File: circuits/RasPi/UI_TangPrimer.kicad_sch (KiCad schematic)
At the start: 10 parts, among them SW6 SW_SPDT

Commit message: PDFプロット
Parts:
- D12, D13, D14, D15: value Red -> Blue
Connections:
- net LED0 renamed LED_B0
- net LED1 renamed LED_B1
- net LED2 renamed LED_B2
- net LED3 renamed LED_B3
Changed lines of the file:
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@@
     (stroke (width 0) (type default))
   )
-  (polyline (pts (xy 106.68 66.04) (xy 170.18 66.04))
+  (polyline (pts (xy 106.68 63.5) (xy 170.18 63.5))
     (stroke (width 0.5) (type solid))
   )
@@
     (stroke (width 0.5) (type solid))
   )
-  (polyline (pts (xy 106.68 147.32) (xy 106.68 66.04))
+  (polyline (pts (xy 106.68 147.32) (xy 106.68 63.5))
     (stroke (width 0.5) (type solid))
   )
-  (polyline (pts (xy 170.18 147.32) (xy 170.18 66.04))
+  (polyline (pts (xy 170.18 147.32) (xy 170.18 63.5))
     (stroke (width 0.5) (type solid))
   )
@@
     (effects (font (size 1.27 1.27)) (justify left bottom))
   )
-  (text "LED" (at 109.22 71.12 0)
+  (text "LED" (at 109.22 68.58 0)
     (effects (font (size 1.27 1.27)) (justify left bottom))
   )
-  (text "I/O" (at 109.22 63.5 0)
+  (text "I/O" (at 109.22 60.96 0)
     (effects (font (size 2.54 2.54)) (justify left bottom))
   )
-  (hierarchical_label "LED2" (shape input) (at 127 93.98 180) (fields_autoplaced)
+  (hierarchical_label "LED_B2" (shape input) (at 127 93.98 180) (fields_autoplaced)
     (effects (font (size 1.27 1.27)) (justify right))
   )
@@
     (effects (font (size 1.27 1.27)) (justify left))
   )
-  (hierarchical_label "LED0" (shape input) (at 127 73.66 180) (fields_autoplaced)
+  (hierarchical_label "LED_B0" (shape input) (at 127 73.66 180) (fields_autoplaced)
     (effects (font (size 1.27 1.27)) (justify right))
   )
-  (hierarchical_label "LED3" (shape input) (at 127 104.14 180) (fields_autoplaced)
+  (hierarchical_label "LED_B3" (shape input) (at 127 104.14 180) (fields_autoplaced)
     (effects (font (size 1.27 1.27)) (justify right))
   )
-  (hierarchical_label "LED1" (shape input) (at 127 83.82 180) (fields_autoplaced)
+  (hierarchical_label "LED_B1" (shape input) (at 127 83.82 180) (fields_autoplaced)
     (effects (font (size 1.27 1.27)) (justify right))
   )
@@
       (effects (font (size 1.27 1.27)))
     )
-    (property "Value" "Red" (at 144.78 96.52 0)
+    (property "Value" "Blue" (at 144.78 96.52 0)
       (effects (font (size 1.27 1.27)))
     )
@@
       (effects (font (size 1.27 1.27)))
     )
-    (property "Value" "Red" (at 144.78 86.36 0)
+    (property "Value" "Blue" (at 144.78 86.36 0)
       (effects (font (size 1.27 1.27)))
     )
@@
       (effects (font (size 1.27 1.27)))
     )
-    (property "Value" "Red" (at 144.78 76.2 0)
+    (property "Value" "Blue" (at 144.78 76.2 0)
       (effects (font (size 1.27 1.27)))
     )
@@
       (effects (font (size 1.27 1.27)))
     )
-    (property "Value" "Red" (at 144.78 106.68 0)
-      (effects (font (size 1.27 1.27)))
-    )
+    (property "Value" "Blue" (at 144.78 106.68 0)
+      (effects (font (size 1.27 1.27)))
+    )

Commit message: シンボル・フットプリントMyLib->TomoshibiLib置き換え
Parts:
- SW6: footprint MyLibrary:SW_Slide_3P_SPDT -> TomoshibiLibrary:SW_Slide_3P_SPDT
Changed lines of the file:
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@@
       (effects (font (size 1.27 1.27)) (justify left))
     )
-    (property "Footprint" "MyLibrary:SW_Slide_3P_SPDT" (at 132.08 129.54 0)
+    (property "Footprint" "TomoshibiLibrary:SW_Slide_3P_SPDT" (at 132.08 129.54 0)
       (effects (font (size 1.27 1.27)) hide)
     )

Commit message: 更新
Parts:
- SW6: footprint TomoshibiLibrary:SW_Slide_3P_SPDT -> TomoshibiLibrary:SW_Slide_SPDT_SSSS213202
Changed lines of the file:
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@@
+    )
+  )
+  (symbol (lib_id "Switch:SW_SPDT") (at 132.08 129.54 0) (mirror x) (unit 1)
+    (in_bom yes) (on_board yes) (dnp no)
+    (property "Reference" "SW6" (at 124.46 136.9314 0)
+      (effects (font (size 1.27 1.27)) (justify left))
+    )
+    (property "Value" "SW_SPDT" (at 124.46 134.62 0)
+      (effects (font (size 1.27 1.27)) (justify left))
+    )
+    (property "Footprint" "TomoshibiLibrary:SW_Slide_SPDT_SSSS213202" (at 132.08 129.54 0)
+      (effects (font (size 1.27 1.27)) hide)
+    )
+    (property "Datasheet" "~" (at 132.08 129.54 0)
+      (effects (font (size 1.27 1.27)) hide)
+    )
+    (pin "1")
+    (pin "2")
+    (pin "3")
+    (instances
+      (project "RasPi"
+        (path "/689a9e74-f202-4ea4-bfbb-4341f2549250/a0e6e20f-c732-4650-b515-927ea2aa6bd5/e4ed8e7b-a26f-475c-8428-58a8505b00cf"
+          (reference "SW6") (unit 1)
+        )
+      )
     )
   )
@@
         )
       )
-    )
-  )
-  (symbol (lib_id "Switch:SW_SPDT") (at 132.08 129.54 0) (mirror x) (unit 1)
-    (in_bom yes) (on_board yes) (dnp no)
-    (property "Reference" "SW6" (at 124.46 136.9314 0)
-      (effects (font (size 1.27 1.27)) (justify left))
-    )
-    (property "Value" "SW_SPDT" (at 124.46 134.62 0)
-      (effects (font (size 1.27 1.27)) (justify left))
-    )
-    (property "Footprint" "TomoshibiLibrary:SW_Slide_3P_SPDT" (at 132.08 129.54 0)
-      (effects (font (size 1.27 1.27)) hide)
-    )
-    (property "Datasheet" "~" (at 132.08 129.54 0)
-      (effects (font (size 1.27 1.27)) hide)
-    )
-    (pin "1")
-    (pin "2")
-    (pin "3")
-    (instances
-      (project "RasPi"
-        (path "/689a9e74-f202-4ea4-bfbb-4341f2549250/a0e6e20f-c732-4650-b515-927ea2aa6bd5/e4ed8e7b-a26f-475c-8428-58a8505b00cf"
-          (reference "SW6") (unit 1)
-        )
-      )

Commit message: raspi基板回路図
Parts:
- added H1, H2, H3, H4: MountingHole_Pad, TestPoint:TestPoint_Pad_1.0x1.0mm, symbol Mechanical:MountingHole_Pad
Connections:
- net LED_B0: now also H1.1
- net LED_B1: now also H2.1
- net LED_B2: now also H3.1
- net LED_B3: now also H4.1
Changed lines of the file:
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@@
 (kicad_sch (version 20230121) (generator eeschema)
   (paper "A4")
+  (junction (at 129.54 93.98) (diameter 0) (color 0 0 0 0)
+  )
   (junction (at 139.7 132.08) (diameter 0) (color 0 0 0 0)
   )
+  (junction (at 129.54 83.82) (diameter 0) (color 0 0 0 0)
+  )
+  (junction (at 129.54 104.14) (diameter 0) (color 0 0 0 0)
+  )
+  (junction (at 129.54 73.66) (diameter 0) (color 0 0 0 0)
+  )
   (no_connect (at 137.16 127))
+  (wire (pts (xy 129.54 83.82) (xy 130.81 83.82))
+    (stroke (width 0) (type default))
+  )
   (wire (pts (xy 124.46 129.54) (xy 127 129.54))
     (stroke (width 0) (type default))
@@
     (stroke (width 0) (type default))
   )
-  (wire (pts (xy 127 93.98) (xy 130.81 93.98))
-    (stroke (width 0) (type default))
-  )
-  (wire (pts (xy 127 83.82) (xy 130.81 83.82))
-    (stroke (width 0) (type default))
-  )
-  (wire (pts (xy 127 104.14) (xy 130.81 104.14))
+  (wire (pts (xy 127 93.98) (xy 129.54 93.98))
+    (stroke (width 0) (type default))
+  )
+  (wire (pts (xy 127 83.82) (xy 129.54 83.82))
+    (stroke (width 0) (type default))
+  )
+  (wire (pts (xy 127 104.14) (xy 129.54 104.14))
     (stroke (width 0) (type default))
   )
@@
     (stroke (width 0.5) (type solid))
   )
+  (wire (pts (xy 129.54 73.66) (xy 130.81 73.66))
+    (stroke (width 0) (type default))
+  )
   (polyline (pts (xy 170.18 147.32) (xy 170.18 63.5))
     (stroke (width 0.5) (type solid))
@@
     (stroke (width 0) (type default))
   )
-  (wire (pts (xy 127 73.66) (xy 130.81 73.66))
+  (wire (pts (xy 129.54 104.14) (xy 130.81 104.14))
+    (stroke (width 0) (type default))
+  )
+  (wire (pts (xy 127 73.66) (xy 129.54 73.66))
+    (stroke (width 0) (type default))
+  )
+  (wire (pts (xy 129.54 93.98) (xy 130.81 93.98))
     (stroke (width 0) (type default))
   )
@@
     )
   )
+  (symbol (lib_id "Mechanical:MountingHole_Pad") (at 129.54 91.44 0) (mirror y) (unit 1)
+    (in_bom yes) (on_board yes) (dnp no)
+    (property "Reference" "H3" (at 114.3 88.9 0)
+      (effects (font (size 1.27 1.27)) (justify right))
+    )
+    (property "Value" "MountingHole_Pad" (at 114.3 86.36 0)
+      (effects (font (size 1.27 1.27)) (justify right))
+    )
+    (property "Footprint" "TestPoint:TestPoint_Pad_1.0x1.0mm" (at 129.54 91.44 0)
+      (effects (font (size 1.27 1.27)) hide)
+    )
+    (property "Datasheet" "~" (at 129.54 91.44 0)
+      (effects (font (size 1.27 1.27)) hide)
+    )
+    (pin "1")
+    (instances
+      (project "RasPi"
+        (path "/689a9e74-f202-4ea4-bfbb-4341f2549250/a0e6e20f-c732-4650-b515-927ea2aa6bd5/e4ed8e7b-a26f-475c-8428-58a8505b00cf"
+          (reference "H3") (unit 1)
+        )
+      )
+    )
+  )
   (symbol (lib_id "power:GNDD") (at 152.4 73.66 0) (unit 1)
     (in_bom yes) (on_board yes) (dnp no) (fields_autoplaced)
@@
     )
   )
+  (symbol (lib_id "Mechanical:MountingHole_Pad") (at 129.54 81.28 0) (mirror y) (unit 1)
+    (in_bom yes) (on_board yes) (dnp no)
+    (property "Reference" "H2" (at 114.3 78.74 0)
+      (effects (font (size 1.27 1.27)) (justify right))
+    )
+    (property "Value" "MountingHole_Pad" (at 114.3 76.2 0)
+      (effects (font (size 1.27 1.27)) (justify right))
+    )
+    (property "Footprint" "TestPoint:TestPoint_Pad_1.0x1.0mm" (at 129.54 81.28 0)
+      (effects (font (size 1.27 1.27)) hide)
+    )
+    (property "Datasheet" "~" (at 129.54 81.28 0)
+      (effects (font (size 1.27 1.27)) hide)
+    )
+    (pin "1")
+    (instances
+      (project "RasPi"
+        (path "/689a9e74-f202-4ea4-bfbb-4341f2549250/a0e6e20f-c732-4650-b515-927ea2aa6bd5/e4ed8e7b-a26f-475c-8428-58a8505b00cf"
+          (reference "H2") (unit 1)
+        )
+      )
+    )
+  )
   (symbol (lib_id "power:GNDD") (at 152.4 83.82 0) (unit 1)
     (in_bom yes) (on_board yes) (dnp no) (fields_autoplaced)
@@
     )
   )
+  (symbol (lib_id "Mechanical:MountingHole_Pad") (at 129.54 101.6 0) (mirror y) (unit 1)
+    (in_bom yes) (on_board yes) (dnp no)
+    (property "Reference" "H4" (at 114.3 99.06 0)
+      (effects (font (size 1.27 1.27)) (justify right))
+    )
+    (property "Value" "MountingHole_Pad" (at 114.3 96.52 0)
+      (effects (font (size 1.27 1.27)) (justify right))
+    )
+    (property "Footprint" "TestPoint:TestPoint_Pad_1.0x1.0mm" (at 129.54 101.6 0)
+      (effects (font (size 1.27 1.27)) hide)
+    )
+    (property "Datasheet" "~" (at 129.54 101.6 0)
+      (effects (font (size 1.27 1.27)) hide)
+    )
+    (pin "1")
+    (instances
+      (project "RasPi"
+        (path "/689a9e74-f202-4ea4-bfbb-4341f2549250/a0e6e20f-c732-4650-b515-927ea2aa6bd5/e4ed8e7b-a26f-475c-8428-58a8505b00cf"
+          (reference "H4") (unit 1)
+        )
+      )
+    )
+  )
   (symbol (lib_id "power:GNDD") (at 154.94 134.62 0) (unit 1)
     (in_bom yes) (on_board yes) (dnp no) (fields_autoplaced)
@@
         )
       )
+    )
+  )
+  (symbol (lib_id "Mechanical:MountingHole_Pad") (at 129.54 71.12 0) (mirror y) (unit 1)
+    (in_bom yes) (on_board yes) (dnp no)
+    (property "Reference" "H1" (at 114.3 68.58 0)
+      (effects (font (size 1.27 1.27)) (justify right))
+    )
+    (property "Value" "MountingHole_Pad" (at 114.3 66.04 0)
+      (effects (font (size 1.27 1.27)) (justify right))
+    )
+    (property "Footprint" "TestPoint:TestPoint_Pad_1.0x1.0mm" (at 129.54 71.12 0)
+      (effects (font (size 1.27 1.27)) hide)
+    )
+    (property "Datasheet" "~" (at 129.54 71.12 0)
+      (effects (font (size 1.27 1.27)) hide)
+    )
+    (pin "1")
+    (instances
+      (project "RasPi"
+        (path "/689a9e74-f202-4ea4-bfbb-4341f2549250/a0e6e20f-c732-4650-b515-927ea2aa6bd5/e4ed8e7b-a26f-475c-8428-58a8505b00cf"
+          (reference "H1") (unit 1)
+        )
+      )

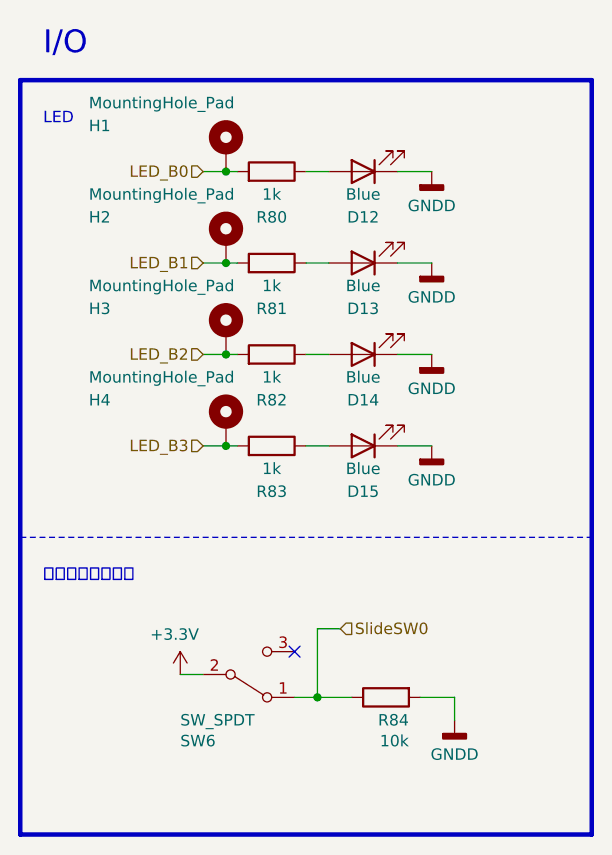
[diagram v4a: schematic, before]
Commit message: 発注第2弾
RasPi発注
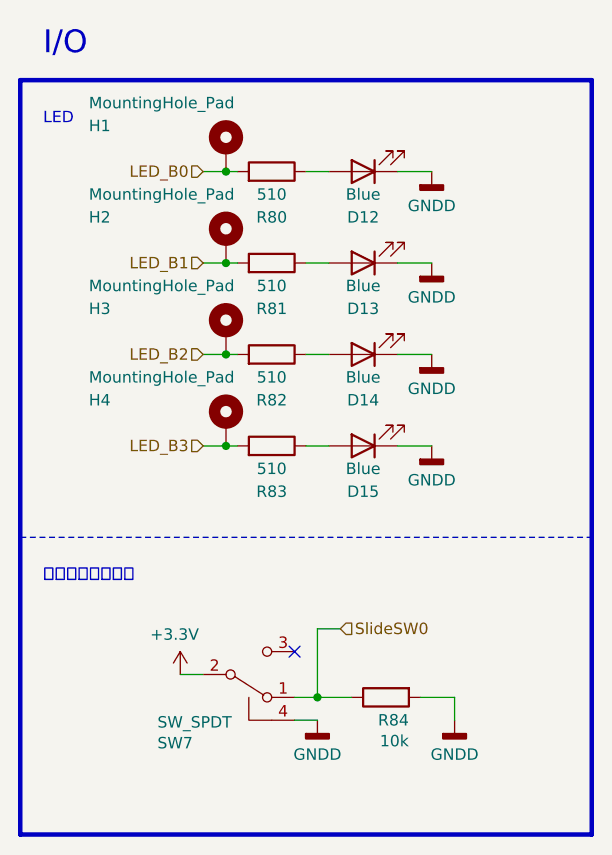
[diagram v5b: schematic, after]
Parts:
- removed SW6: SW_SPDT, TomoshibiLibrary:SW_Slide_SPDT_SSSS213202, symbol Switch:SW_SPDT
- added SW7: SW_SPDT, TomoshibiLibrary:SW_Slide_DPDT_SSSS820101, symbol Switch:SW_SPDT
- R80, R81, R82, R83: value 1k -> 510
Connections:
- net +3.3V: now also SW7.2 (B)
- net GNDD: now also SW7.4, SW7.5 (shell), SW7.6 (shell), SW7.G1 (shell), SW7.G2 (shell), SW7.G3 (shell), SW7.G4 (shell)
- net SlideSW0: now also SW7.1 (A)
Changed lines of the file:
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@@
+    (stroke (width 0) (type default))
+  )
+  (wire (pts (xy 137.16 134.62) (xy 139.7 134.62))
     (stroke (width 0) (type default))
   )
@@
     )
   )
+  (symbol (lib_name "SW_SPDT_1") (lib_id "Switch:SW_SPDT") (at 132.08 129.54 0) (mirror x) (unit 1)
+    (in_bom yes) (on_board yes) (dnp no)
+    (property "Reference" "SW7" (at 121.92 137.16 0)
+      (effects (font (size 1.27 1.27)) (justify left))
+    )
+    (property "Value" "SW_SPDT" (at 121.92 134.8486 0)
+      (effects (font (size 1.27 1.27)) (justify left))
+    )
+    (property "Footprint" "TomoshibiLibrary:SW_Slide_DPDT_SSSS820101" (at 132.08 129.54 0)
+      (effects (font (size 1.27 1.27)) hide)
+    )
+    (property "Datasheet" "~" (at 132.08 129.54 0)
+      (effects (font (size 1.27 1.27)) hide)
+    )
+    (pin "1")
+    (pin "2")
+    (pin "3")
+    (pin "4")
+    (pin "5")
+    (pin "6")
+    (pin "G2")
+    (pin "G1")
+    (pin "G3")
+    (pin "G4")
+    (instances
+      (project "RasPi"
+        (path "/689a9e74-f202-4ea4-bfbb-4341f2549250/a0e6e20f-c732-4650-b515-927ea2aa6bd5/e4ed8e7b-a26f-475c-8428-58a8505b00cf"
+          (reference "SW7") (unit 1)
+        )
+      )
+    )
+  )
+  (symbol (lib_id "power:GNDD") (at 139.7 134.62 0) (unit 1)
+    (in_bom yes) (on_board yes) (dnp no) (fields_autoplaced)
+    (property "Reference" "#PWR0103" (at 139.7 140.97 0)
+      (effects (font (size 1.27 1.27)) hide)
+    )
+    (property "Value" "GNDD" (at 139.7 138.43 0)
+      (effects (font (size 1.27 1.27)))
+    )
+    (property "Footprint" "" (at 139.7 134.62 0)
+      (effects (font (size 1.27 1.27)) hide)
+    )
+    (property "Datasheet" "" (at 139.7 134.62 0)
+      (effects (font (size 1.27 1.27)) hide)
+    )
+    (pin "1")
+    (instances
+      (project "RasPi"
+        (path "/689a9e74-f202-4ea4-bfbb-4341f2549250/a0e6e20f-c732-4650-b515-927ea2aa6bd5/e4ed8e7b-a26f-475c-8428-58a8505b00cf"
+          (reference "#PWR0103") (unit 1)
+        )
+      )
+    )
+  )
   (symbol (lib_id "Device:LED") (at 144.78 93.98 180) (unit 1)
     (in_bom yes) (on_board yes) (dnp no)
@@
       (effects (font (size 1.27 1.27)))
     )
-    (property "Value" "1k" (at 134.62 96.52 90)
+    (property "Value" "510" (at 134.62 96.52 90)
       (effects (font (size 1.27 1.27)))
     )
@@
       (effects (font (size 1.27 1.27)))
     )
-    (property "Value" "1k" (at 134.62 86.36 90)
+    (property "Value" "510" (at 134.62 86.36 90)
       (effects (font (size 1.27 1.27)))
     )
@@
     )
   )
-  (symbol (lib_id "Switch:SW_SPDT") (at 132.08 129.54 0) (mirror x) (unit 1)
-    (in_bom yes) (on_board yes) (dnp no)
-    (property "Reference" "SW6" (at 124.46 136.9314 0)
-      (effects (font (size 1.27 1.27)) (justify left))
-    )
-    (property "Value" "SW_SPDT" (at 124.46 134.62 0)
-      (effects (font (size 1.27 1.27)) (justify left))
-    )
-    (property "Footprint" "TomoshibiLibrary:SW_Slide_SPDT_SSSS213202" (at 132.08 129.54 0)
-      (effects (font (size 1.27 1.27)) hide)
-    )
-    (property "Datasheet" "~" (at 132.08 129.54 0)
-      (effects (font (size 1.27 1.27)) hide)
-    )
-    (pin "1")
-    (pin "2")
-    (pin "3")
-    (instances
-      (project "RasPi"
-        (path "/689a9e74-f202-4ea4-bfbb-4341f2549250/a0e6e20f-c732-4650-b515-927ea2aa6bd5/e4ed8e7b-a26f-475c-8428-58a8505b00cf"
-          (reference "SW6") (unit 1)
-        )
-      )
-    )
-  )
   (symbol (lib_id "power:+3.3V") (at 124.46 129.54 0) (unit 1)
     (in_bom yes) (on_board yes) (dnp no)
@@
       (effects (font (size 1.27 1.27)))
     )
-    (property "Value" "1k" (at 134.62 76.2 90)
+    (property "Value" "510" (at 134.62 76.2 90)
       (effects (font (size 1.27 1.27)))
     )
@@
       (effects (font (size 1.27 1.27)))
     )
-    (property "Value" "1k" (at 134.62 106.68 90)
-      (effects (font (size 1.27 1.27)))
-    )
+    (property "Value" "510" (at 134.62 106.68 90)
+      (effects (font (size 1.27 1.27)))
+    )
